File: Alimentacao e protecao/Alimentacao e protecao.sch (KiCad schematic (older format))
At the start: 20 parts, among them J1 PinoCheckBateriaVcc, J2 PinoCheckBateriaGND, J3 8.4V_PlacaCentral, J4 GND_PlacaCentral, Q1 BC548, Q2 BC548, SW1 SW_ON/OFF

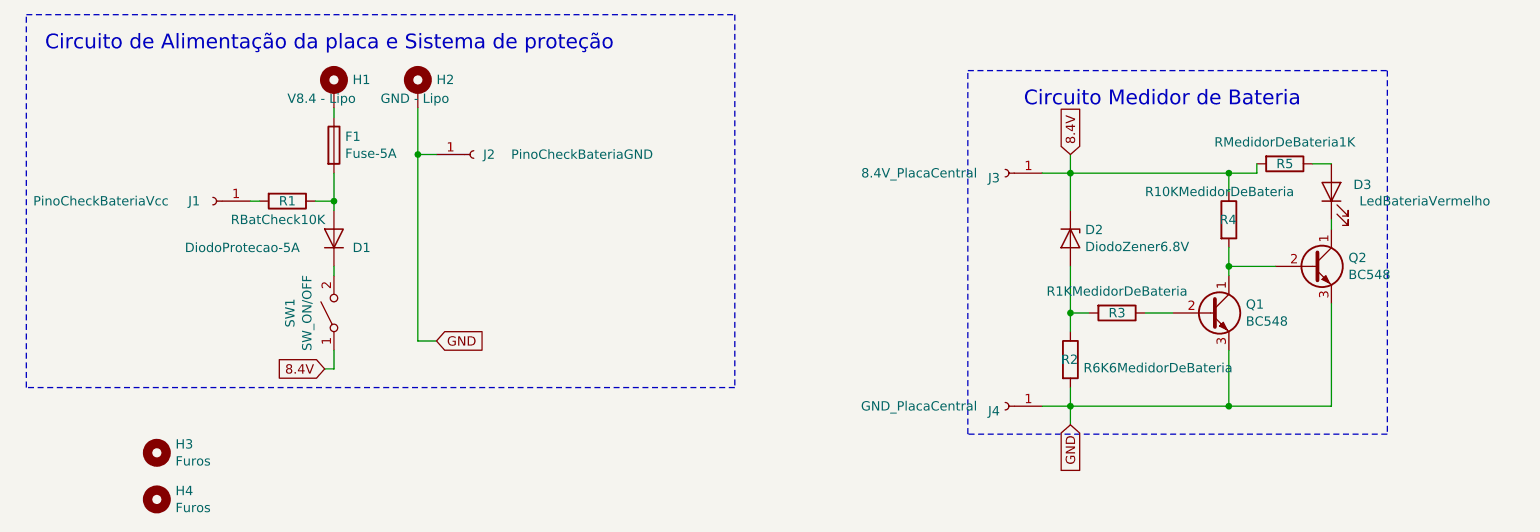
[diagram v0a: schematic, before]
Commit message: Acertada as placas e os pdfs
Acertada as placas centrais, de alimentação e de conector.
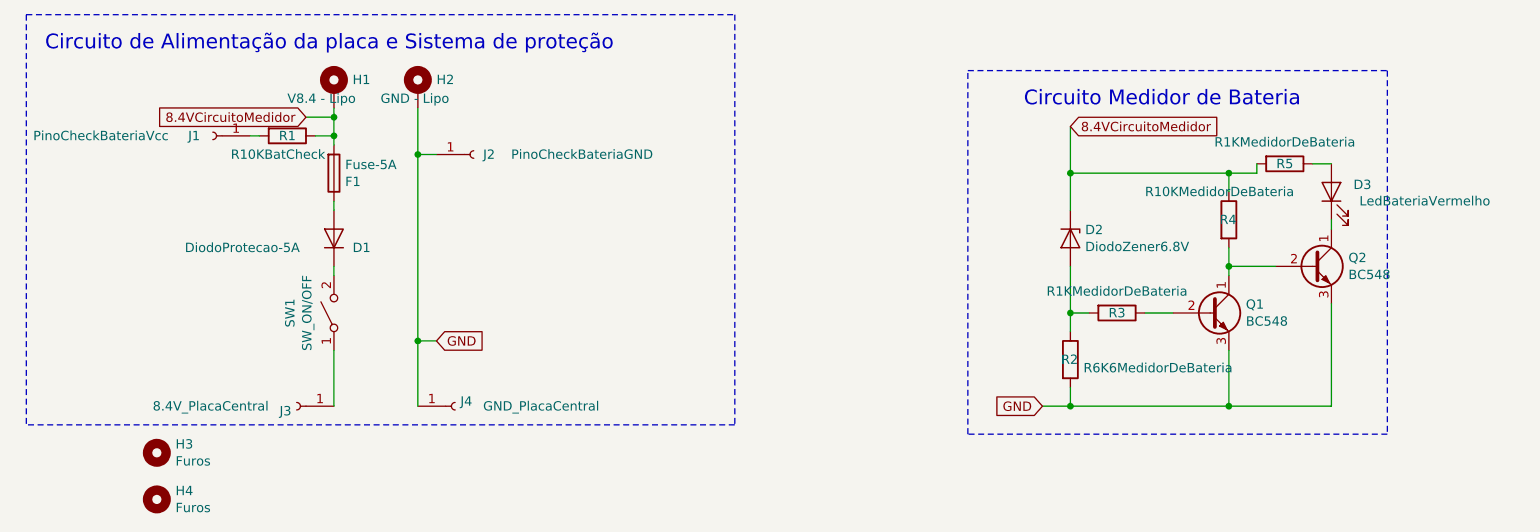
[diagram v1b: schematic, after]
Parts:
- R1: value RBatCheck10K -> R10KBatCheck
- R5: value RMedidorDeBateria1K -> R1KMedidorDeBateria
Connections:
- net at F1.1: now also D1.2 (A); no longer H1.1
- net 8.4VCircuitoMedidor: now reaches F1.2, R1.1
- net 8.4VCircuitoMedidor: now also D2.1 (K), H1.1, R4.1, R5.2; no longer D1.2 (A)
- removed net 8.4V: D2.1 (K), J3.1 (Pin_1), R4.1, R5.2, SW1.1 (A)
- new net: J3.1 (Pin_1), SW1.1 (A)
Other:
- moved on the sheet: F1, J1, J3, J4, R1
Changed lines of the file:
@@
 EESchema Schematic File Version 4
 LIBS:Alimentacao e protecao-cache
-EELAYER 30 0
+EELAYER 29 0
 EELAYER END
 $Descr A4 11693 8268
@@
 L Device:Fuse F1
 U 1 1 5D154189
-P 2850 2000
-F 0 "F1" H 2910 2046 50  0000 L CNN
-F 1 "Fuse-5A" H 2910 1955 50  0000 L CNN
-F 2 "Fuse:Fuseholder_Cylinder-5x20mm_Stelvio-Kontek_PTF78_Horizontal_Open" V 2780 2000 50  0001 C CNN
-F 3 "~" H 2850 2000 50  0001 C CNN
-	1    2850 2000
-	1    0    0    -1
-$EndComp
-Wire Wire Line
-	2850 1800 2850 1850
-Wire Wire Line
-	2850 3100 2850 3200
-Wire Wire Line
-	2850 3200 2800 3200
+P 2850 2150
+F 0 "F1" H 2910 2196 50  0000 L CNN
+F 1 "Fuse-5A" H 2910 2105 50  0000 L CNN
+F 2 "Fuse:Fuseholder_Cylinder-5x20mm_Stelvio-Kontek_PTF78_Horizontal_Open" V 2780 2150 50  0001 C CNN
+F 3 "~" H 2850 2150 50  0001 C CNN
+	1    2850 2150
+	1    0    0    1
+$EndComp
 Wire Wire Line
 	3300 3050 3400 3050
@@
 Circuito de Alimentação da placa e Sistema de proteção
 Wire Notes Line
-	1200 3300 1200 1300
-Wire Notes Line
-	5000 1300 5000 3300
-Wire Notes Line
 	1200 1300 5000 1300
 Wire Notes Line
-	5000 3300 1200 3300
+	5000 3500 1200 3500
 Wire Wire Line
 	2850 2650 2850 2700
-$Comp
-L Connector:Conn_01x01_Female J1
-U 1 1 5D20493D
-P 2200 2300
-F 0 "J1" H 2300 2300 50  0000 C CNN
-F 1 "PinoCheckBateriaVcc" H 2800 2300 50  0000 C CNN
-F 2 "Connector_PinSocket_2.54mm:PinSocket_1x01_P2.54mm_Vertical" H 2200 2300 50  0001 C CNN
-F 3 "~" H 2200 2300 50  0001 C CNN
-	1    2200 2300
-	-1   0    0    1
-$EndComp
-Wire Wire Line
-	2750 2300 2850 2300
-Wire Wire Line
-	2850 2350 2850 2300
-Connection ~ 2850 2300
 $Comp
 L Device:D_Zener D2
@@
 P 7950 2100
 F 0 "R5" V 7950 2100 50  0000 C CNN
-F 1 "RMedidorDeBateria1K" V 7834 2100 50  0000 C CNN
+F 1 "R1KMedidorDeBateria" V 7834 2100 50  0000 C CNN
 F 2 "Resistor_THT:R_Axial_DIN0207_L6.3mm_D2.5mm_P10.16mm_Horizontal" V 7880 2100 50  0001 C CNN
 F 3 "~" H 7950 2100 50  0001 C CNN
@@
 $EndComp
 Wire Wire Line
-	6650 3400 6800 3400
-Wire Wire Line
 	6800 3400 6800 3300
 Wire Wire Line
@@
 Wire Wire Line
 	8200 3400 7650 3400
-Connection ~ 6800 3400
-Wire Wire Line
-	7650 3400 6800 3400
 Connection ~ 7650 3400
 Wire Wire Line
@@
 Wire Wire Line
 	7650 2150 7800 2150
-Wire Wire Line
-	6650 2150 6800 2150
 Wire Wire Line
 	6800 2350 6800 2150
@@
 	6250 1600 8500 1600
 Wire Wire Line
-	2400 2300 2450 2300
-Wire Wire Line
 	3300 2050 3300 3050
-$Comp
-L Device:R R1
-U 1 1 5D1A4675
-P 2600 2300
-F 0 "R1" V 2600 2300 50  0000 C CNN
-F 1 "RBatCheck10K" V 2700 2250 50  0000 C CNN
-F 2 "Resistor_THT:R_Axial_DIN0207_L6.3mm_D2.5mm_P10.16mm_Horizontal" V 2530 2300 50  0001 C CNN
-F 3 "~" H 2600 2300 50  0001 C CNN
-	1    2600 2300
-	0    1    1    0
-$EndComp
-Wire Wire Line
-	2850 2150 2850 2300
 $Comp
 L Connector:Conn_01x01_Female J3
 U 1 1 5D3D07BC
-P 6450 2150
-F 0 "J3" H 6478 2176 50  0000 L CNN
-F 1 "8.4V_PlacaCentral" H 6600 2150 50  0000 L CNN
-F 2 "Connector_Wire:SolderWirePad_1x01_Drill1.2mm" H 6450 2150 50  0001 C CNN
-F 3 "~" H 6450 2150 50  0001 C CNN
-	1    6450 2150
+P 2650 3400
+F 0 "J3" H 2678 3426 50  0000 L CNN
+F 1 "8.4V_PlacaCentral" H 2800 3400 50  0000 L CNN
+F 2 "Connector_Wire:SolderWirePad_1x01_Drill1.2mm" H 2650 3400 50  0001 C CNN
+F 3 "~" H 2650 3400 50  0001 C CNN
+	1    2650 3400
 	-1   0    0    1
 $EndComp
@@
 L Connector:Conn_01x01_Female J4
 U 1 1 5D3D515E
-P 6450 3400
-F 0 "J4" H 6478 3426 50  0000 L CNN
-F 1 "GND_PlacaCentral" H 6600 3400 50  0000 L CNN
-F 2 "Connector_Wire:SolderWirePad_1x01_Drill1.2mm" H 6450 3400 50  0001 C CNN
-F 3 "~" H 6450 3400 50  0001 C CNN
-	1    6450 3400
-	-1   0    0    1
-$EndComp
-Text GLabel 2800 3200 0    50   Input ~ 0
-8.4V
+P 3500 3400
+F 0 "J4" H 3528 3426 50  0000 L CNN
+F 1 "GND_PlacaCentral" H 3650 3400 50  0000 L CNN
+F 2 "Connector_Wire:SolderWirePad_1x01_Drill1.2mm" H 3500 3400 50  0001 C CNN
+F 3 "~" H 3500 3400 50  0001 C CNN
+	1    3500 3400
+	1    0    0    -1
+$EndComp
 Text GLabel 3400 3050 2    50   Input ~ 0
 GND
-Text GLabel 6800 2050 1    50   Input ~ 0
-8.4V
-Wire Wire Line
-	6800 2050 6800 2150
-Text GLabel 6800 3500 3    50   Input ~ 0
+Text GLabel 6650 3400 0    50   Input ~ 0
 GND
-Wire Wire Line
-	6800 3500 6800 3400
 $Comp
 L Mechanical:MountingHole H3
@@
 	1    0    0    -1
 $EndComp
+$Comp
+L Connector:Conn_01x01_Female J1
+U 1 1 5D20493D
+P 2200 1950
+F 0 "J1" H 2300 1950 50  0000 C CNN
+F 1 "PinoCheckBateriaVcc" H 2800 1950 50  0000 C CNN
+F 2 "Connector_PinSocket_2.54mm:PinSocket_1x01_P2.54mm_Vertical" H 2200 1950 50  0001 C CNN
+F 3 "~" H 2200 1950 50  0001 C CNN
+	1    2200 1950
+	-1   0    0    1
+$EndComp
+Wire Wire Line
+	2400 1950 2450 1950
+$Comp
+L Device:R R1
+U 1 1 5D1A4675
+P 2600 1950
+F 0 "R1" V 2600 1950 50  0000 C CNN
+F 1 "R10KBatCheck" V 2700 1900 50  0000 C CNN
+F 2 "Resistor_THT:R_Axial_DIN0207_L6.3mm_D2.5mm_P10.16mm_Horizontal" V 2530 1950 50  0001 C CNN
+F 3 "~" H 2600 1950 50  0001 C CNN
+	1    2600 1950
+	0    1    1    0
+$EndComp
+Wire Wire Line
+	2750 1950 2850 1950
+Wire Wire Line
+	2850 1800 2850 1850
+Wire Wire Line
+	2850 1950 2850 2000
+Connection ~ 2850 1950
+Wire Wire Line
+	2850 2300 2850 2350
+Text GLabel 2700 1850 0    50   Input ~ 0
+8.4VCircuitoMedidor
+Wire Wire Line
+	2700 1850 2850 1850
+Connection ~ 2850 1850
+Wire Wire Line
+	2850 1850 2850 1950
+Text GLabel 6800 1900 2    50   Input ~ 0
+8.4VCircuitoMedidor
+Wire Wire Line
+	6800 1900 6800 2150
+Wire Notes Line
+	5000 1300 5000 3500
+Wire Notes Line
+	1200 1300 1200 3500
+Wire Wire Line
+	2850 3100 2850 3400
+Wire Wire Line
+	3300 3400 3300 3050
+Connection ~ 3300 3050
+Wire Wire Line
+	7650 3400 6800 3400
+Wire Wire Line
+	6650 3400 6800 3400
+Connection ~ 6800 3400
 $EndSCHEMATC
